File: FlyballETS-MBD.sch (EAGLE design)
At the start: 16 parts, among them Q1 BC557, Q2 BC557

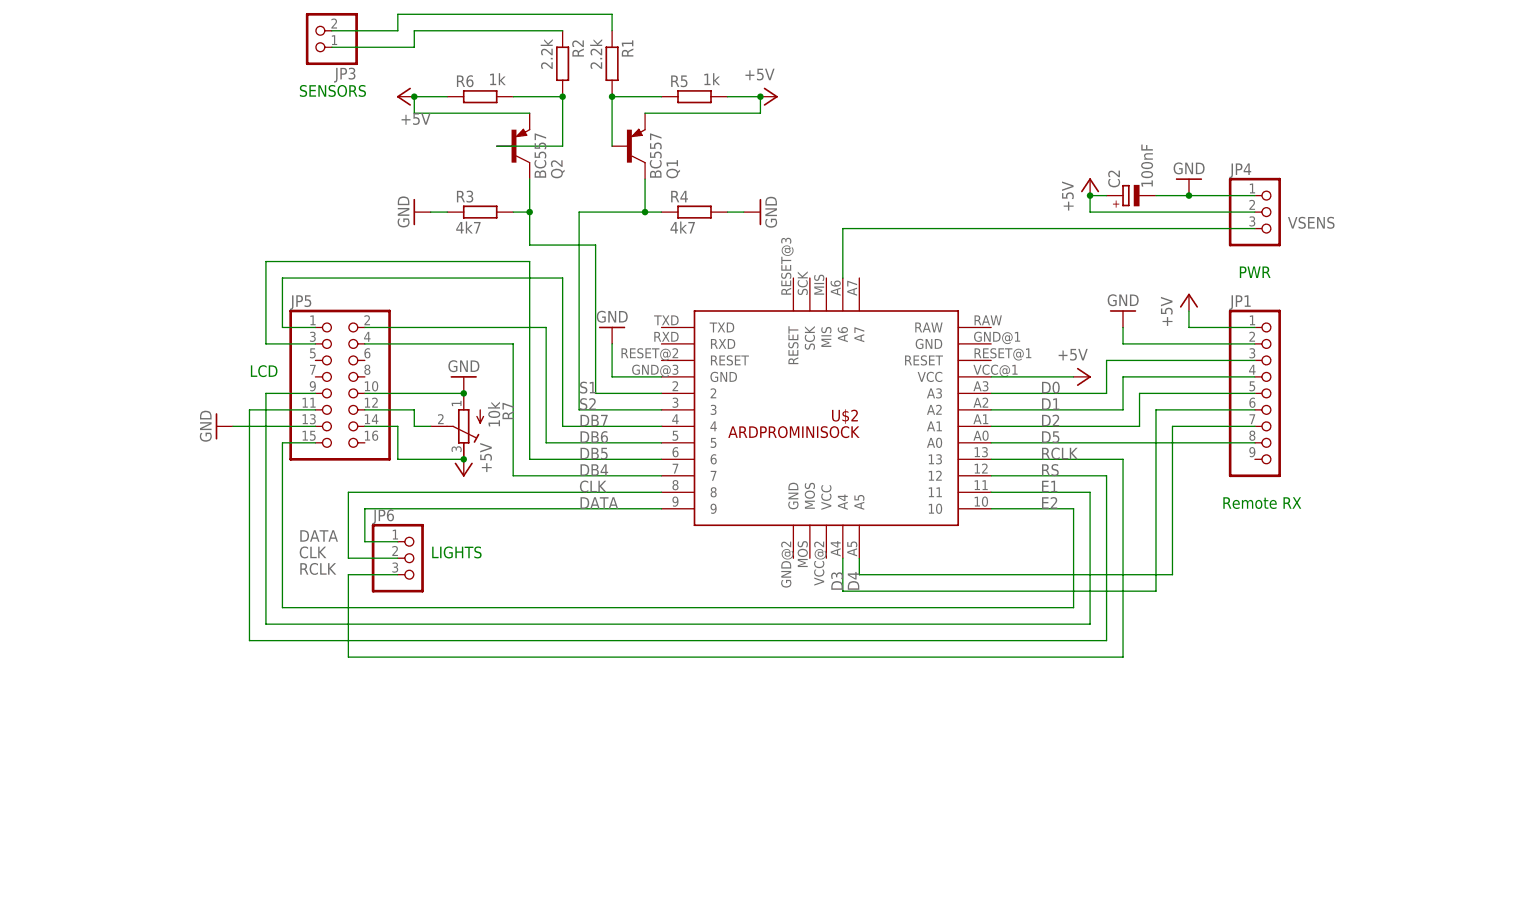
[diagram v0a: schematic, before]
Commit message: Updated drawings and added PNG exports
- Added frames around drawings to make it look neater
- Added PNG export files so people who don't have EAGLE can see
everything
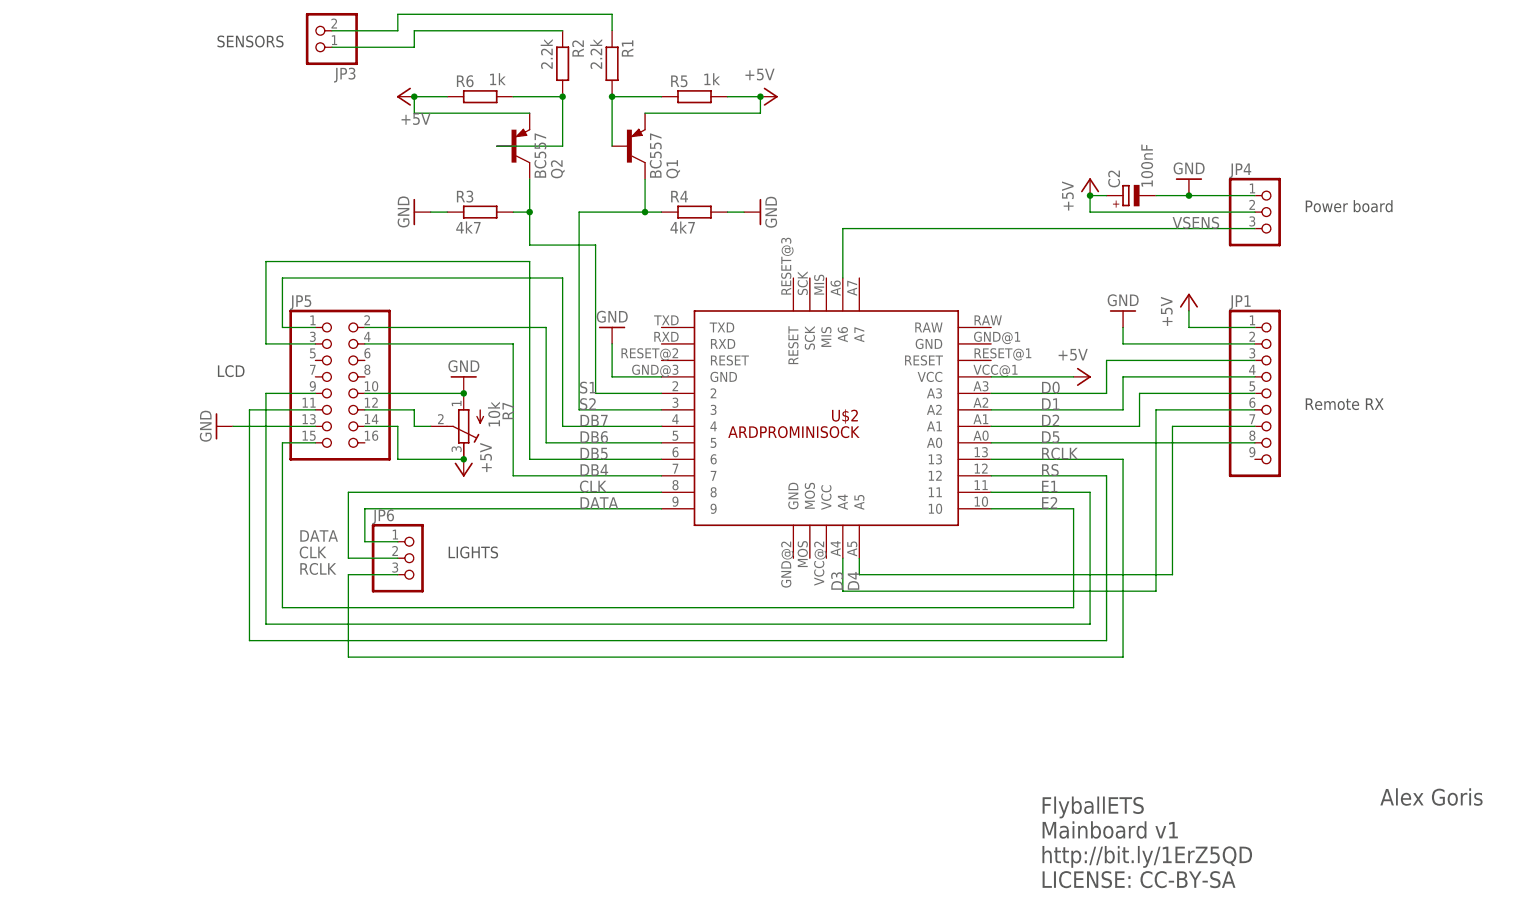
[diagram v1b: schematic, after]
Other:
- note added: "Alex Goris"
- note added: "FlyballETS Mainboard v1 http://bit.ly/1ErZ5QD LICENSE: CC-BY-SA"
- note added: "Power board"
- note removed: "PWR"
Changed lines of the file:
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@@
 <schematic xreflabel="%F%N/%S.%C%R" xrefpart="/%S.%C%R">
 <attributes>
+<attribute name="CNAME" value="Alex Goris"/>
 </attributes>
 <variantdefs>
@@
 <part name="C2" library="resistor" deviceset="CPOL-EU" device="E2,5-6E" value="100nF"/>
 <part name="U$2" library="_custom" deviceset="ARDPROMINISOCK" device=""/>
+<part name="FRAME1" library="frames" deviceset="A4L-LOC" device=""/>
 </parts>
 <sheets>
 <sheet>
 <plain>
-<text x="154.94" y="76.2" size="1.778" layer="91">Remote RX</text>
-<text x="157.48" y="111.76" size="1.778" layer="91">PWR</text>
-<text x="5.08" y="96.52" size="1.778" layer="91">LCD</text>
-<text x="33.02" y="68.58" size="1.778" layer="91">LIGHTS</text>
-<text x="12.7" y="139.7" size="1.778" layer="91">SENSORS</text>
+<text x="167.64" y="91.44" size="1.778" layer="97">Remote RX</text>
+<text x="167.64" y="121.92" size="1.778" layer="97">Power board</text>
+<text x="0" y="96.52" size="1.778" layer="97">LCD</text>
+<text x="35.56" y="68.58" size="1.778" layer="97">LIGHTS</text>
+<text x="0" y="147.32" size="1.778" layer="97">SENSORS</text>
+<text x="127" y="17.78" size="2.54" layer="97">FlyballETS
+Mainboard v1
+http://bit.ly/1ErZ5QD
+LICENSE: CC-BY-SA</text>
+<text x="179.324" y="30.48" size="2.54" layer="97">Alex Goris</text>
 </plain>
 <instances>
@@
 <instance part="C2" gate="G$1" x="139.7" y="124.46" rot="R90"/>
 <instance part="U$2" gate="G$1" x="114.3" y="106.68" rot="R180"/>
+<instance part="FRAME1" gate="G$1" x="-38.1" y="10.16"/>
 </instances>
 <busses>
@@
 <segment>
 <pinref part="JP4" gate="A" pin="3"/>
-<label x="165.1" y="119.38" size="1.778" layer="95"/>
+<label x="147.32" y="119.38" size="1.778" layer="95"/>
 <pinref part="U$2" gate="G$1" pin="A6"/>
 <wire x1="160.02" y1="119.38" x2="96.52" y2="119.38" width="0.1524" layer="91"/>
@@
 </schematic>
 </drawing>
+<compatibility>
+<note version="6.3" minversion="6.2.2" severity="warning">
+Since Version 6.2.2 text objects can contain more than one line,
+which will not be processed correctly with this version.
+</note>
+</compatibility>
 </eagle>

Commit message: Mainboard v2
- Changed connectors to use JST-XH type
- For LCD screen use flatcable/ribboncable connector (2x9 pins)
- Repositioned everything to allow for smaller board size (12% smaller)
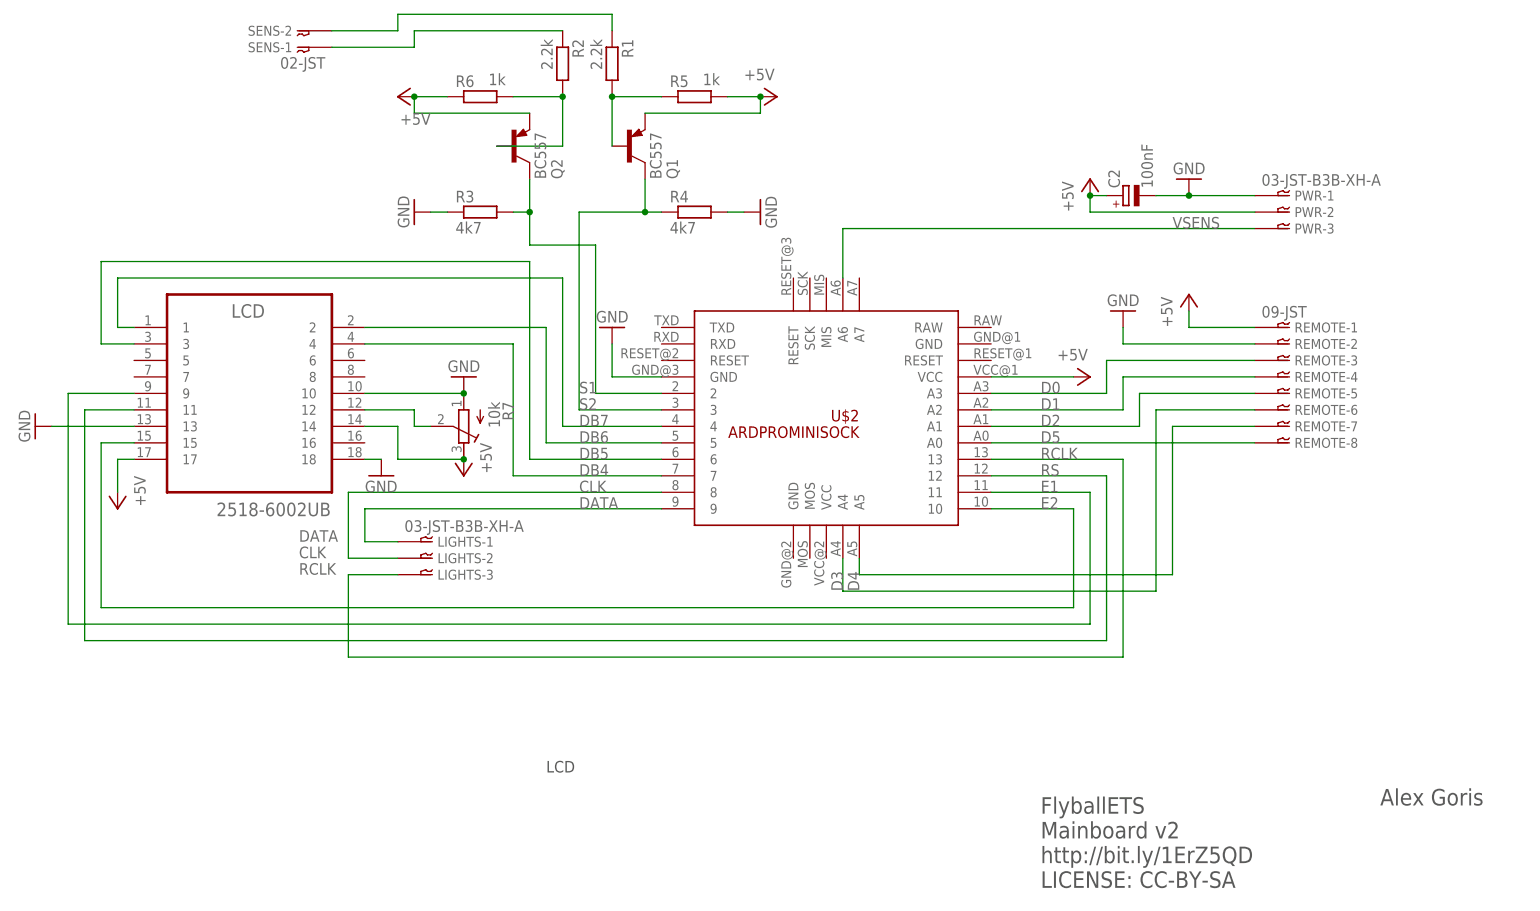
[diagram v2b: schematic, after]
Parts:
- removed JP1: (no value), pinhead:PINHD-1X9
- removed JP3: (no value), pinhead:PINHD-1X2
- removed JP4, JP6: (no value), pinhead:PINHD-1X3
- removed JP5: (no value), pinhead:PINHD-2X8
- added LCD: 2518-6002UB, 3M_By_element14_Batch_1:2518-6002UB
- added LIGHTS, PWR: 03-JST-B3B-XH-A, bt_con-jst-xh:03-JST-B3B-XH-A
- added REMOTE: 09-JST, bt_con-jst-xh:09-JST
- added SENS: 02-JST, bt_con-jst-xh:02-JST
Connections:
- net +5V: now also LCD.14, LCD.17, PWR-2.1, REMOTE-1.1; no longer JP1.1, JP4.2, JP5.14
- net CLK: now also LIGHTS-2.1; no longer JP6.2
- net D0: now also REMOTE-3.1; no longer JP1.3
- net D1: now also REMOTE-4.1; no longer JP1.4
- net D2: now also REMOTE-5.1; no longer JP1.5
- net D3: now also REMOTE-6.1; no longer JP1.6
- net D4: now also REMOTE-7.1; no longer JP1.7
- net D5: now also REMOTE-8.1; no longer JP1.8
- net DATA: now also LIGHTS-1.1; no longer JP6.1
- net DB4: now also LCD.4; no longer JP5.4
- net DB5: now also LCD.3; no longer JP5.3
- net DB6: now also LCD.2; no longer JP5.2
- net DB7: now also LCD.1; no longer JP5.1
- net E1: now also LCD.9; no longer JP5.9
- net E2: now also LCD.15; no longer JP5.15
- net GND: now also LCD.10, LCD.13, LCD.18, PWR-1.1, REMOTE-2.1; no longer JP1.2, JP4.1, JP5.10, JP5.13
- net N$1: now also SENS-2.1; no longer JP3.2
- net N$2: now also SENS-1.1; no longer JP3.1
- net N$5: now also LCD.12; no longer JP5.12
- net RCLK: now also LIGHTS-3.1; no longer JP6.3
- net RS: now also LCD.11; no longer JP5.11
- net VSENS: now also PWR-3.1; no longer JP4.3
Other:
- note added: "FlyballETS Mainboard v2 http://bit.ly/1ErZ5QD LICENSE: CC-BY-SA"
- note removed: "FlyballETS Mainboard v1 http://bit.ly/1ErZ5QD LICENSE: CC-BY-SA"
- note removed: "LIGHTS"
- note removed: "Power board"
- note removed: "Remote RX"
- note removed: "SENSORS"

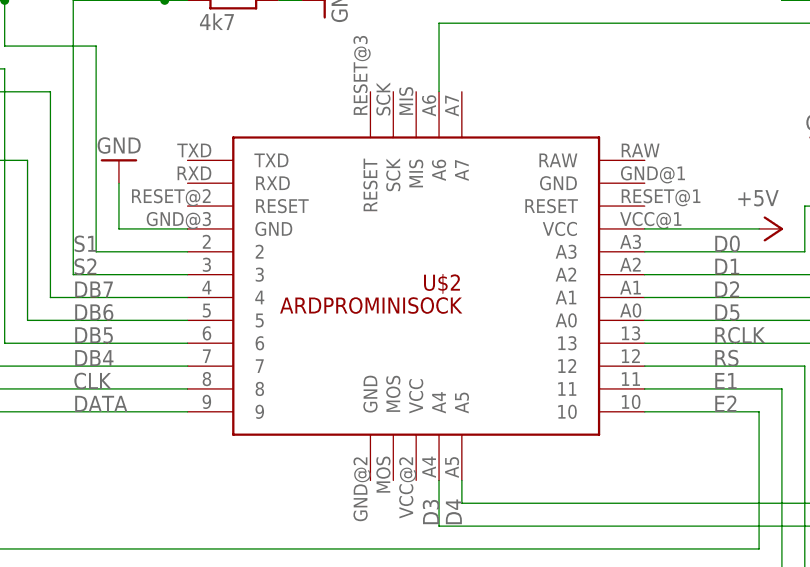
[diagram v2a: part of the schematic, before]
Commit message: Minor updates + added BOMs
- Updated to EAGLE 7.5.0
- Added BOM text file exports
- Renamed arduino socket on MBD board
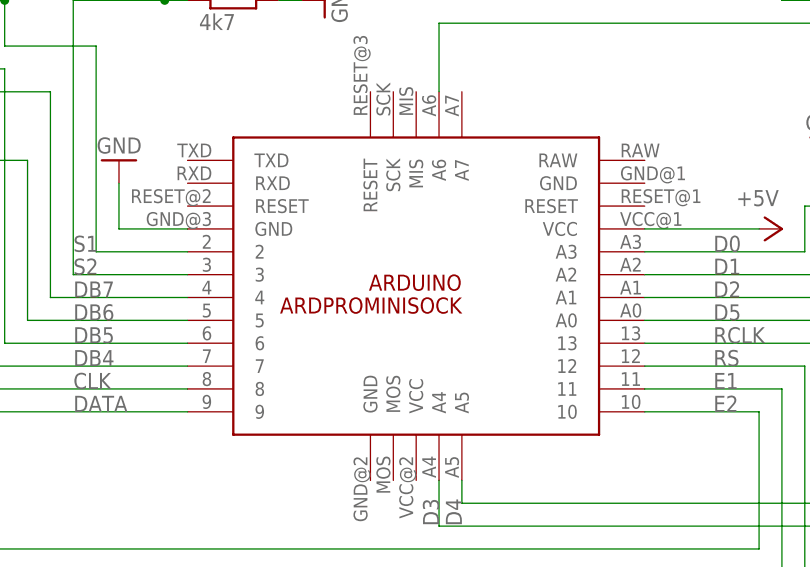
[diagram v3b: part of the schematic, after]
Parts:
- renumbered U$2 to ARDUINO
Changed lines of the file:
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@@
 <?xml version="1.0" encoding="utf-8"?>
 <!DOCTYPE eagle SYSTEM "eagle.dtd">
-<eagle version="7.4.0">
+<eagle version="7.5.0">
 <drawing>
 <settings>
@@
 <part name="GND7" library="supply1" deviceset="GND" device=""/>
 <part name="C2" library="resistor" deviceset="CPOL-EU" device="E2,5-6E" value="100nF"/>
-<part name="U$2" library="_custom" deviceset="ARDPROMINISOCK" device=""/>
+<part name="ARDUINO" library="_custom" deviceset="ARDPROMINISOCK" device=""/>
 <part name="FRAME1" library="frames" deviceset="A4L-LOC" device=""/>
 <part name="LCD" library="3M_By_element14_Batch_1" deviceset="2518-6002UB" device=""/>
@@
 <instance part="GND7" gate="1" x="149.86" y="127" rot="R180"/>
 <instance part="C2" gate="G$1" x="139.7" y="124.46" rot="R90"/>
-<instance part="U$2" gate="G$1" x="114.3" y="106.68" rot="R180"/>
+<instance part="ARDUINO" gate="G$1" x="114.3" y="106.68" rot="R180"/>
 <instance part="FRAME1" gate="G$1" x="-38.1" y="10.16"/>
 <instance part="LCD" gate="G$1" x="5.08" y="96.52" smashed="yes">
@@
 <pinref part="GND6" gate="1" pin="GND"/>
 <wire x1="60.96" y1="96.52" x2="60.96" y2="101.6" width="0.1524" layer="91"/>
-<pinref part="U$2" gate="G$1" pin="GND@3"/>
+<pinref part="ARDUINO" gate="G$1" pin="GND@3"/>
 </segment>
 <segment>
@@
 <wire x1="137.16" y1="99.06" x2="160.02" y2="99.06" width="0.1524" layer="91"/>
 <label x="127" y="93.98" size="1.778" layer="95"/>
-<pinref part="U$2" gate="G$1" pin="A3"/>
+<pinref part="ARDUINO" gate="G$1" pin="A3"/>
 <pinref part="REMOTE" gate="-3" pin="1"/>
 </segment>
@@
 <pinref part="P+5" gate="1" pin="+5V"/>
 <wire x1="119.38" y1="96.52" x2="132.08" y2="96.52" width="0.1524" layer="91"/>
-<pinref part="U$2" gate="G$1" pin="VCC@1"/>
+<pinref part="ARDUINO" gate="G$1" pin="VCC@1"/>
 </segment>
 <segment>
@@
 <wire x1="139.7" y1="96.52" x2="160.02" y2="96.52" width="0.1524" layer="91"/>
 <label x="127" y="91.44" size="1.778" layer="95"/>
-<pinref part="U$2" gate="G$1" pin="A2"/>
+<pinref part="ARDUINO" gate="G$1" pin="A2"/>
 <pinref part="REMOTE" gate="-4" pin="1"/>
 </segment>
@@
 <wire x1="160.02" y1="93.98" x2="142.24" y2="93.98" width="0.1524" layer="91"/>
 <label x="127" y="88.9" size="1.778" layer="95"/>
-<pinref part="U$2" gate="G$1" pin="A1"/>
+<pinref part="ARDUINO" gate="G$1" pin="A1"/>
 <pinref part="REMOTE" gate="-5" pin="1"/>
 </segment>
@@
 <wire x1="144.78" y1="91.44" x2="144.78" y2="63.5" width="0.1524" layer="91"/>
 <wire x1="144.78" y1="63.5" x2="96.52" y2="63.5" width="0.1524" layer="91"/>
-<pinref part="U$2" gate="G$1" pin="A4"/>
+<pinref part="ARDUINO" gate="G$1" pin="A4"/>
 <wire x1="96.52" y1="63.5" x2="96.52" y2="68.58" width="0.1524" layer="91"/>
 <label x="96.52" y="63.5" size="1.778" layer="95" rot="R90"/>
@@
 <wire x1="147.32" y1="88.9" x2="147.32" y2="66.04" width="0.1524" layer="91"/>
 <wire x1="147.32" y1="66.04" x2="99.06" y2="66.04" width="0.1524" layer="91"/>
-<pinref part="U$2" gate="G$1" pin="A5"/>
+<pinref part="ARDUINO" gate="G$1" pin="A5"/>
 <wire x1="99.06" y1="66.04" x2="99.06" y2="68.58" width="0.1524" layer="91"/>
 <label x="99.06" y="63.5" size="1.778" layer="95" rot="R90"/>
@@
 <label x="127" y="86.36" size="1.778" layer="95"/>
 <wire x1="119.38" y1="86.36" x2="160.02" y2="86.36" width="0.1524" layer="91"/>
-<pinref part="U$2" gate="G$1" pin="A0"/>
+<pinref part="ARDUINO" gate="G$1" pin="A0"/>
 <pinref part="REMOTE" gate="-8" pin="1"/>
 </segment>
@@
 <wire x1="119.38" y1="78.74" x2="134.62" y2="78.74" width="0.1524" layer="91"/>
 <label x="127" y="78.74" size="1.778" layer="95"/>
-<pinref part="U$2" gate="G$1" pin="11"/>
+<pinref part="ARDUINO" gate="G$1" pin="11"/>
 <pinref part="LCD" gate="G$1" pin="9"/>
 </segment>
@@
 <wire x1="137.16" y1="55.88" x2="137.16" y2="81.28" width="0.1524" layer="91"/>
 <label x="127" y="81.28" size="1.778" layer="95"/>
-<pinref part="U$2" gate="G$1" pin="12"/>
+<pinref part="ARDUINO" gate="G$1" pin="12"/>
 <wire x1="137.16" y1="81.28" x2="119.38" y2="81.28" width="0.1524" layer="91"/>
 <pinref part="LCD" gate="G$1" pin="11"/>
@@
 <wire x1="119.38" y1="76.2" x2="132.08" y2="76.2" width="0.1524" layer="91"/>
 <label x="127" y="76.2" size="1.778" layer="95"/>
-<pinref part="U$2" gate="G$1" pin="10"/>
+<pinref part="ARDUINO" gate="G$1" pin="10"/>
 <pinref part="LCD" gate="G$1" pin="15"/>
 </segment>
@@
 <label x="55.88" y="76.2" size="1.778" layer="95"/>
 <wire x1="22.86" y1="76.2" x2="68.58" y2="76.2" width="0.1524" layer="91"/>
-<pinref part="U$2" gate="G$1" pin="9"/>
+<pinref part="ARDUINO" gate="G$1" pin="9"/>
 <label x="12.7" y="71.12" size="1.778" layer="95"/>
 <pinref part="LIGHTS" gate="-1" pin="1"/>
@@
 <label x="55.88" y="78.74" size="1.778" layer="95"/>
 <wire x1="20.32" y1="78.74" x2="68.58" y2="78.74" width="0.1524" layer="91"/>
-<pinref part="U$2" gate="G$1" pin="8"/>
+<pinref part="ARDUINO" gate="G$1" pin="8"/>
 <label x="12.7" y="68.58" size="1.778" layer="95"/>
 <pinref part="LIGHTS" gate="-2" pin="1"/>
@@
 <wire x1="139.7" y1="53.34" x2="139.7" y2="83.82" width="0.1524" layer="91"/>
 <label x="127" y="83.82" size="1.778" layer="95"/>
-<pinref part="U$2" gate="G$1" pin="13"/>
+<pinref part="ARDUINO" gate="G$1" pin="13"/>
 <wire x1="139.7" y1="83.82" x2="119.38" y2="83.82" width="0.1524" layer="91"/>
 <label x="12.7" y="66.04" size="1.778" layer="95"/>
@@
 <wire x1="68.58" y1="91.44" x2="55.88" y2="91.44" width="0.1524" layer="91"/>
 <label x="55.88" y="91.44" size="1.778" layer="95"/>
-<pinref part="U$2" gate="G$1" pin="3"/>
+<pinref part="ARDUINO" gate="G$1" pin="3"/>
 </segment>
 </net>
@@
 <wire x1="68.58" y1="93.98" x2="58.42" y2="93.98" width="0.1524" layer="91"/>
 <label x="55.88" y="93.98" size="1.778" layer="95"/>
-<pinref part="U$2" gate="G$1" pin="2"/>
+<pinref part="ARDUINO" gate="G$1" pin="2"/>
 </segment>
 </net>
@@
 <wire x1="53.34" y1="88.9" x2="53.34" y2="111.76" width="0.1524" layer="91"/>
 <label x="55.88" y="88.9" size="1.778" layer="95"/>
-<pinref part="U$2" gate="G$1" pin="4"/>
+<pinref part="ARDUINO" gate="G$1" pin="4"/>
 <wire x1="53.34" y1="111.76" x2="-15.24" y2="111.76" width="0.1524" layer="91"/>
 <wire x1="-15.24" y1="111.76" x2="-15.24" y2="104.14" width="0.1524" layer="91"/>
@@
 <wire x1="48.26" y1="114.3" x2="48.26" y2="83.82" width="0.1524" layer="91"/>
 <label x="55.88" y="83.82" size="1.778" layer="95"/>
-<pinref part="U$2" gate="G$1" pin="6"/>
+<pinref part="ARDUINO" gate="G$1" pin="6"/>
 <wire x1="48.26" y1="83.82" x2="68.58" y2="83.82" width="0.1524" layer="91"/>
 <wire x1="-17.78" y1="114.3" x2="-17.78" y2="101.6" width="0.1524" layer="91"/>
@@
 <wire x1="50.8" y1="104.14" x2="22.86" y2="104.14" width="0.1524" layer="91"/>
 <label x="55.88" y="86.36" size="1.778" layer="95"/>
-<pinref part="U$2" gate="G$1" pin="5"/>
+<pinref part="ARDUINO" gate="G$1" pin="5"/>
 <pinref part="LCD" gate="G$1" pin="2"/>
 </segment>
@@
 <wire x1="45.72" y1="101.6" x2="22.86" y2="101.6" width="0.1524" layer="91"/>
 <label x="55.88" y="81.28" size="1.778" layer="95"/>
-<pinref part="U$2" gate="G$1" pin="7"/>
+<pinref part="ARDUINO" gate="G$1" pin="7"/>
 <pinref part="LCD" gate="G$1" pin="4"/>
 </segment>
@@
 <segment>
 <label x="147.32" y="119.38" size="1.778" layer="95"/>
-<pinref part="U$2" gate="G$1" pin="A6"/>
+<pinref part="ARDUINO" gate="G$1" pin="A6"/>
 <wire x1="160.02" y1="119.38" x2="96.52" y2="119.38" width="0.1524" layer="91"/>
 <wire x1="96.52" y1="119.38" x2="96.52" y2="111.76" width="0.1524" layer="91"/>
